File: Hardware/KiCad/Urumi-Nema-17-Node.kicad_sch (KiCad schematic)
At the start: 48 parts, among them J1 Screw_Terminal_01x02_P3.5mm, J2 Limit Switch, J3 395016004, J4 B4B-XH-A_LF__SN_, J5 B4B-XH-A_LF__SN_, J8 PinHeader_01x05_P2.54mm_Horiz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, M0 SolderJumper_2_Open, M1 SolderJumper_2_Open, M2 SolderJumper_2_Open, Q2 SS8050, SW1 Switch_Tactile_CnK, U1 Microcontroller_AVR128DB32-I_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, U3 DRV8825_STEPPER_MOTOR_DRIVER_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, U5 MAX485E, Y1 16_MHz_Crystal

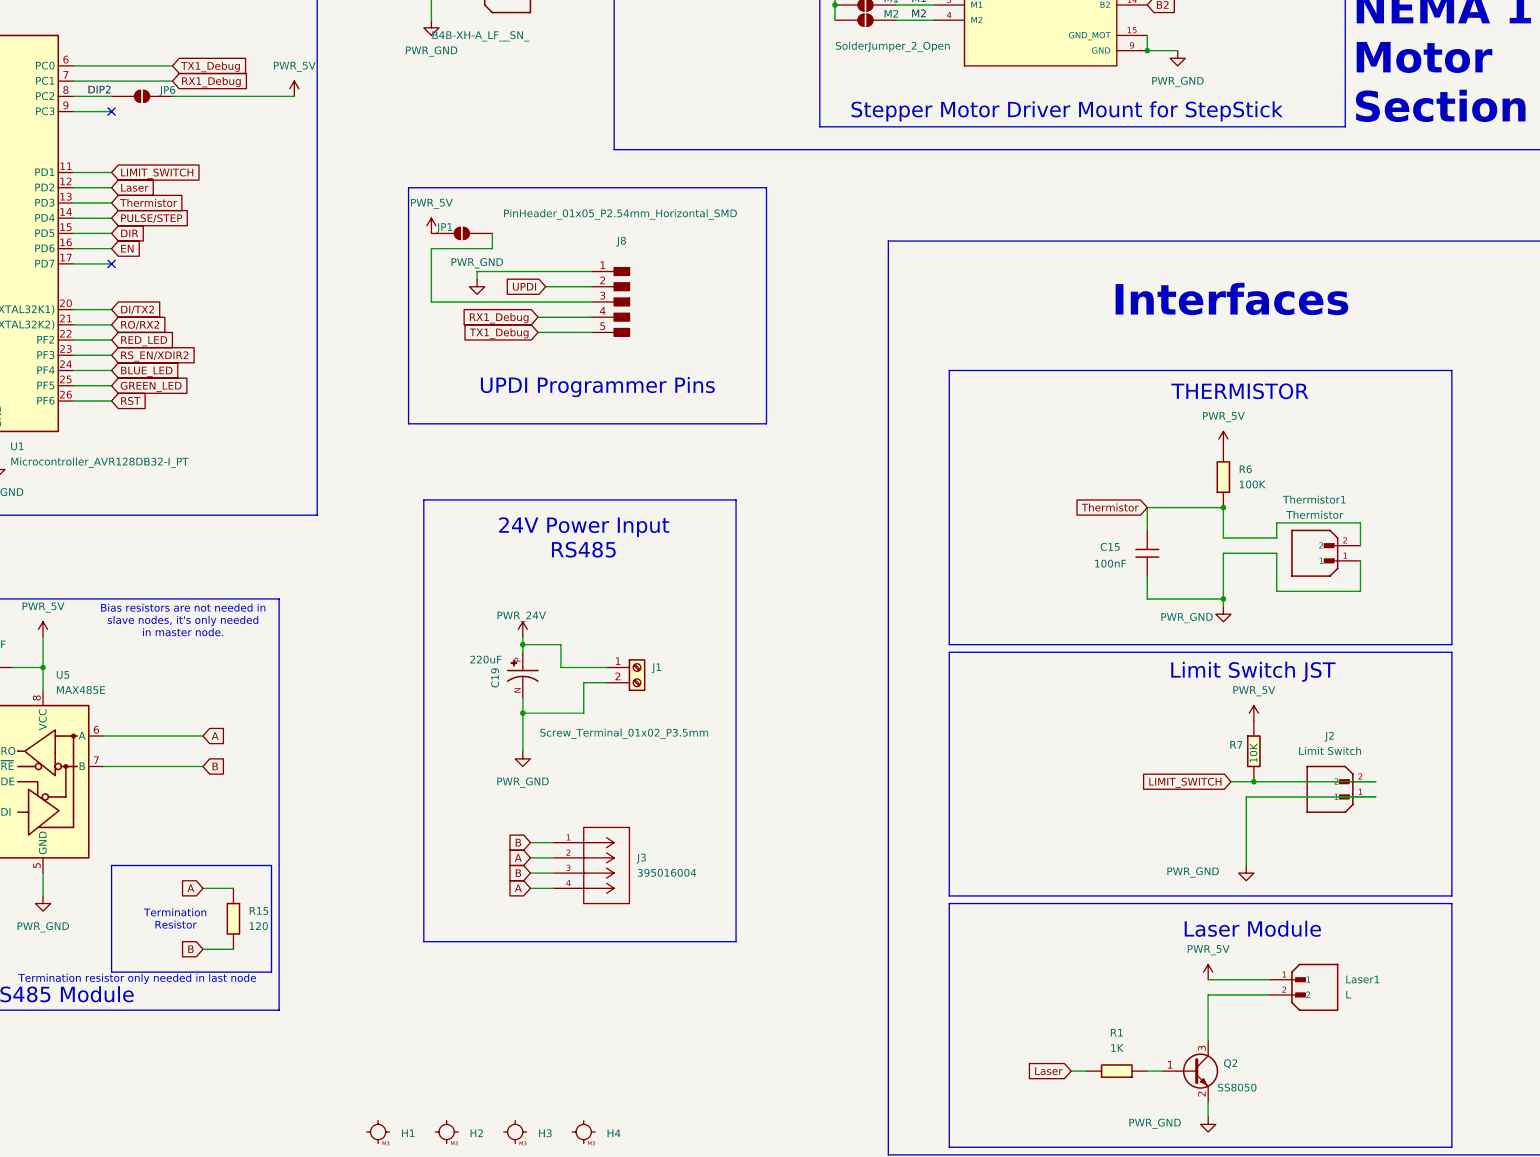
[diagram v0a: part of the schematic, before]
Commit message: hw: v2.2a PCB with in and out terminals, just one debug led- no rgb
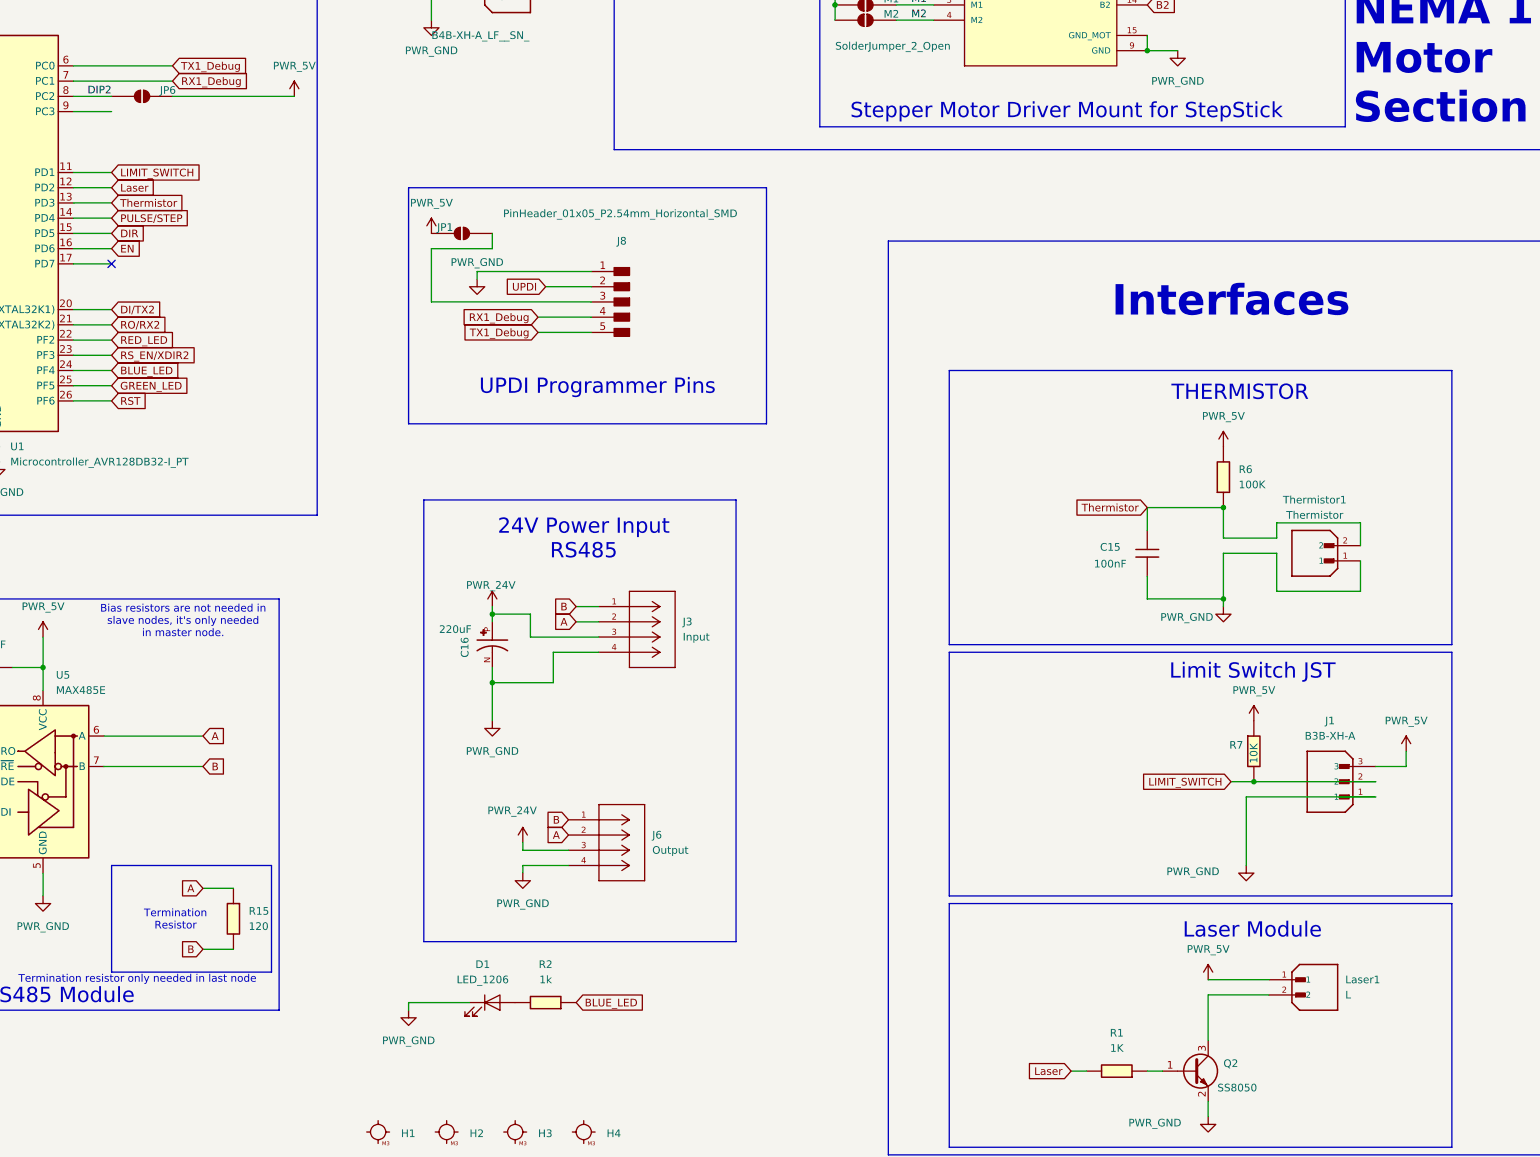
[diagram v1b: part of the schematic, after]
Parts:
- removed C19: 220uF, EEUFS1H221LB:CAPPRD500W60D800H2000, symbol EEUFS1H221LB:EEUFS1H221LB
- removed J1: Screw_Terminal_01x02_P3.5mm, fab:TerminalBlock_OnShore_1x02_P3.50mm_Horizontal, symbol fab:Screw_Terminal_01x02_P3.5mm
- removed J2: Limit Switch, B2B-XH-A_LF__SN_:JST_B2B-XH-A_LF__SN_, symbol B2B-XH-A_LF__SN_:B2B-XH-A_LF__SN_
- added C16: 220uF, EEUFS1H221LB:CAPPRD500W60D800H2000, symbol EEUFS1H221LB:EEUFS1H221LB
- added D1: LED_1206, PCM_fab:LED_1206, symbol PCM_fab:LED_1206
- added J1: B3B-XH-A, fab:JST_B3B-XH-A, symbol B3B-XH-A:B3B-XH-A
- added J6: Output, 4 Pin:CONN_SD-39501-001_04P_MOL, symbol 395016004:395016004
- added R2: 1k, Resistor_SMD:R_0805_2012Metric_Pad1.20x1.40mm_HandSolder, symbol PCM_fab:R_1206
- J3: value 395016004 -> Input
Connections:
- net A: now also J6.2; no longer J3.4
- net B: now also J6.1; no longer J3.3
- net BLUE_LED: now also R2.2
- net LIMIT_SWITCH: now also J1.2
- net PWR_24V: now also J3.3, C16.P, J6.3
- net PWR_5V: now also J1.3
- net PWR_GND: now also J3.4, C16.N, D1.1 (K), J1.1, J6.4
- new net: D1.2 (A), R2.1
- no-connect marks 2 -> 1
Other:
- moved on the sheet: J3

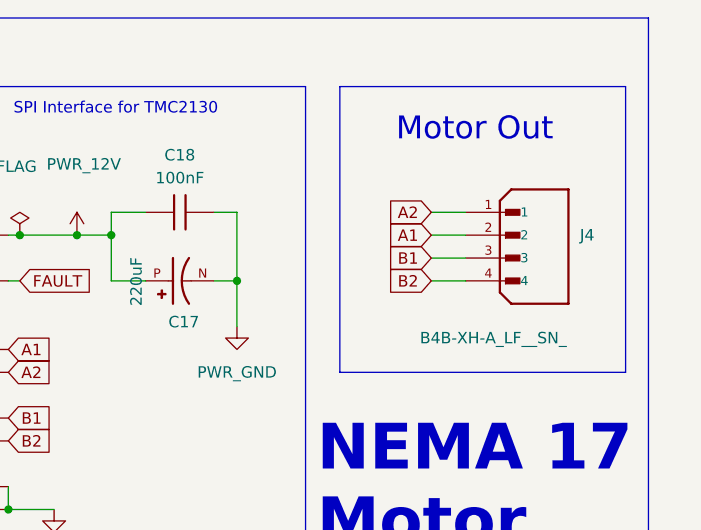
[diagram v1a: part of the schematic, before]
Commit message: hw: v2.2a correct one JST - final V2.2a
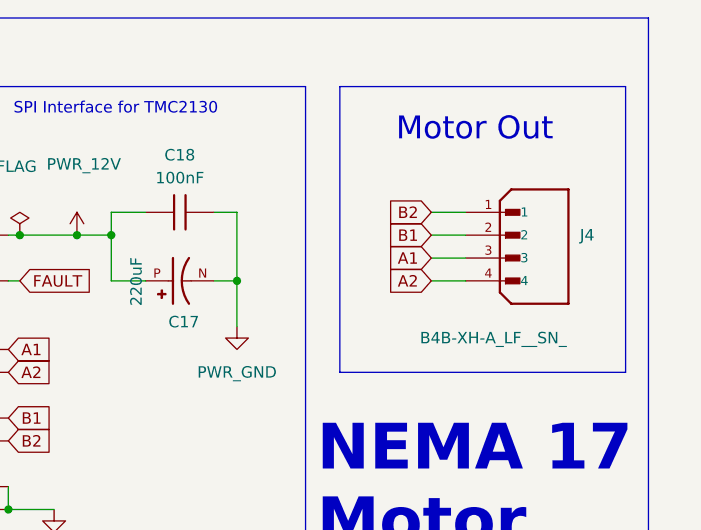
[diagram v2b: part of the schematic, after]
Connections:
- net A1: now also J4.3; no longer J4.2
- net A2: now also J4.4; no longer J4.1
- net B1: now also J4.2; no longer J4.3
- net B2: now also J4.1; no longer J4.4

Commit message: hw: v1.0.1 corrected major mistake - didn't connect to driver to 24V
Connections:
- net PWR_12V is gone; now on net PWR_24V: C17.P, C18.1, U3.16 (VMOT)
- no-connect marks 1 -> 2

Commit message: hw:v1.1.0
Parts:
- D3, R10, R11, R9: now not fitted
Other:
- note added: "DM542 Output"
- note added: "Debug LED"
- moved on the sheet: D1, R2
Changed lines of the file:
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@@
 	)
 	(rectangle
+		(start 198.12 35.56)
+		(end 238.76 74.93)
+		(stroke
+			(width 0)
+			(type default)
+		)
+		(fill
+			(type none)
+		)
+	)
+	(rectangle
 		(start 102.87 158.75)
 		(end 187.96 227.33)
@@
 	(rectangle
 		(start 12.7 193.04)
-		(end 78.74 228.6)
+		(end 78.74 259.08)
 		(stroke
 			(width 0)
@@
 	)
 	(rectangle
+		(start 17.78 231.14)
+		(end 71.12 254)
+		(stroke
+			(width 0)
+			(type default)
+		)
+		(fill
+			(type none)
+		)
+	)
+	(rectangle
 		(start 278.13 20.32)
 		(end 365.76 80.01)
@@
 		)
 	)
+	(text "Debug LED\n"
+		(exclude_from_sim no)
+		(at 54.61 250.698 0)
+		(effects
+			(font
+				(size 2.54 2.54)
+			)
+		)
+	)
 	(text "Termination resistor only needed in last node"
 		(exclude_from_sim no)
@@
 		)
 	)
+	(text "DM542 Output\n"
+		(exclude_from_sim no)
+		(at 218.694 40.132 0)
+		(effects
+			(font
+				(size 2.54 2.54)
+				(thickness 0.508)
+				(bold yes)
+			)
+		)
+	)
 	(text "24V Power Input\nRS485\n\n"
 		(exclude_from_sim no)
@@
 	(wire
 		(pts
-			(xy 209.55 226.06) (xy 209.55 227.33)
+			(xy 26.67 241.3) (xy 26.67 242.57)
 		)
 		(stroke
@@
 	(wire
 		(pts
-			(xy 219.71 226.06) (xy 209.55 226.06)
+			(xy 36.83 241.3) (xy 26.67 241.3)
 		)
 		(stroke
@@
 	(global_label "BLUE_LED"
 		(shape input)
-		(at 237.49 226.06 0)
+		(at 54.61 241.3 0)
 		(fields_autoplaced yes)
 		(effects
@@
 		)
 		(property "Intersheetrefs" "${INTERSHEET_REFS}"
-			(at 249.6675 226.06 0)
+			(at 66.7875 241.3 0)
 			(hide yes)
 			(show_name no)
@@
 		(on_board no)
 		(in_pos_files yes)
-		(dnp no)
+		(dnp yes)
 		(property "Reference" "D3"
 			(at 58.42 204.47 0)
@@
 	(symbol
 		(lib_id "PCM_fab:R_1206")
-		(at 232.41 226.06 90)
+		(at 49.53 241.3 90)
 		(unit 1)
 		(body_style 1)
@@
 		(dnp no)
 		(property "Reference" "R2"
-			(at 232.41 219.71 90)
+			(at 49.53 234.95 90)
 			(show_name no)
 			(do_not_autoplace no)
@@
 		)
 		(property "Value" "1k"
-			(at 232.41 222.25 90)
+			(at 49.53 237.49 90)
 			(show_name no)
 			(do_not_autoplace no)
@@
 		)
 		(property "Footprint" "Resistor_SMD:R_0805_2012Metric_Pad1.20x1.40mm_HandSolder"
-			(at 250.19 232.918 90)
+			(at 67.31 248.158 90)
 			(hide yes)
 			(show_name no)
@@
 		)
 		(property "Datasheet" ""
-			(at 232.41 226.06 0)
+			(at 49.53 241.3 0)
 			(hide yes)
 			(show_name no)
@@
 		)
 		(property "Description" "Resistor"
-			(at 232.41 226.06 0)
+			(at 49.53 241.3 0)
 			(hide yes)
 			(show_name no)
@@
 	(symbol
 		(lib_id "fab:PWR_GND")
-		(at 209.55 227.33 0)
+		(at 26.67 242.57 0)
 		(unit 1)
 		(body_style 1)
@@
 		(fields_autoplaced yes)
 		(property "Reference" "#PWR010"
-			(at 209.55 233.68 0)
+			(at 26.67 248.92 0)
 			(hide yes)
 			(show_name no)
@@
 		)
 		(property "Value" "PWR_GND"
-			(at 209.55 232.41 0)
+			(at 26.67 247.65 0)
 			(show_name no)
 			(do_not_autoplace no)
@@
 		)
 		(property "Footprint" ""
-			(at 209.55 227.33 0)
+			(at 26.67 242.57 0)
 			(hide yes)
 			(show_name no)
@@
 		)
 		(property "Datasheet" ""
-			(at 209.55 227.33 0)
+			(at 26.67 242.57 0)
 			(hide yes)
 			(show_name no)
@@
 		)
 		(property "Description" "Power symbol creates a global label with name \"GND\" , ground"
-			(at 209.55 227.33 0)
+			(at 26.67 242.57 0)
 			(hide yes)
 			(show_name no)
@@
 		(exclude_from_sim no)
 		(in_bom yes)
-		(on_board yes)
+		(on_board no)
 		(in_pos_files yes)
-		(dnp no)
+		(dnp yes)
 		(fields_autoplaced yes)
 		(property "Reference" "#PWR017"
@@
 		(on_board no)
 		(in_pos_files yes)
-		(dnp no)
+		(dnp yes)
 		(property "Reference" "R9"
 			(at 36.322 210.82 90)
@@
 		(on_board no)
 		(in_pos_files yes)
-		(dnp no)
+		(dnp yes)
 		(property "Reference" "R10"
 			(at 39.37 218.694 90)
@@
 		(on_board no)
 		(in_pos_files yes)
-		(dnp no)
+		(dnp yes)
 		(property "Reference" "R11"
 			(at 39.624 203.708 90)
@@
 	(symbol
 		(lib_id "PCM_fab:LED_1206")
-		(at 223.52 226.06 0)
+		(at 40.64 241.3 0)
 		(unit 1)
 		(body_style 1)
@@
 		(fields_autoplaced yes)
 		(property "Reference" "D1"
-			(at 221.9198 219.71 0)
+			(at 39.0398 234.95 0)
 			(show_name no)
 			(do_not_autoplace no)
@@
 		)
 		(property "Value" "LED_1206"
-			(at 221.9198 222.25 0)
+			(at 39.0398 237.49 0)
 			(show_name no)
 			(do_not_autoplace no)
@@
 		)
 		(property "Footprint" "PCM_fab:LED_1206"
-			(at 223.52 226.06 0)
+			(at 40.64 241.3 0)
 			(hide yes)
 			(show_name no)
@@
 		)
 		(property "Datasheet" "https://optoelectronics.liteon.com/upload/download/DS-22-98-0002/LTST-C150CKT.pdf"
-			(at 223.52 226.06 0)
+			(at 40.64 241.3 0)
 			(hide yes)
 			(show_name no)
@@
 		)
 		(property "Description" "Light emitting diode, Lite-On Inc. LTST, SMD"
-			(at 223.52 226.06 0)
+			(at 40.64 241.3 0)
 			(hide yes)
 			(show_name no)

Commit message: hw: added test points and renders, cad
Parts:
- added TP1, TP10, TP11, TP12, TP13, TP14, TP2, TP3, TP4, TP5, TP6, TP7, TP8, TP9: TestPoint, TestPoint:TestPoint_Pad_1.0x1.0mm, symbol Connector:TestPoint
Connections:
- net A: now also TP6.1
- net B: now also TP7.1
- net CS: now also TP14.1
- net DI/TX2: now also TP5.1
- net LIMIT_SWITCH: now also TP12.1
- net PWR_24V: now also TP1.1
- net PWR_5V: now also TP2.1
- net PWR_GND: now also TP10.1, TP8.1, TP9.1
- net RO/RX2: now also TP4.1
- net RS_EN/XDIR2: now also TP3.1
- net SDI/MOSI: now also TP13.1
- net Thermistor: now also TP11.1

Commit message: hw: final V1.1.0
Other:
- moved on the sheet: C15, J1, R6, R7, TP11, TP12, Thermistor1

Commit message: added docs
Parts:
- Y1: value 16_MHz_Crystal -> 24_MHz_Crystal
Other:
- note added: "24 Mhz Crystal"
- note removed: "16 Mhz Crystal"
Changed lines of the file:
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@@
 		)
 	)
-	(text "16 Mhz Crystal"
+	(text "24 Mhz Crystal"
 		(exclude_from_sim no)
 		(at 44.704 87.376 0)
@@
 			)
 		)
-		(property "Value" "16_MHz_Crystal"
+		(property "Value" "24_MHz_Crystal"
 			(at 36.068 125.73 0)
 			(show_name no)
